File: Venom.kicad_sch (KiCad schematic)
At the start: 12 parts, among them CN1 HC-XH-5A-G, CN2 HC-PH-8A-G, CN3 HC-XH-8A-G, CN4 HC-XH-8A-G, CN5 HC-XH-2A-G, CN6 HC-PH-7A-G, U1 Pico

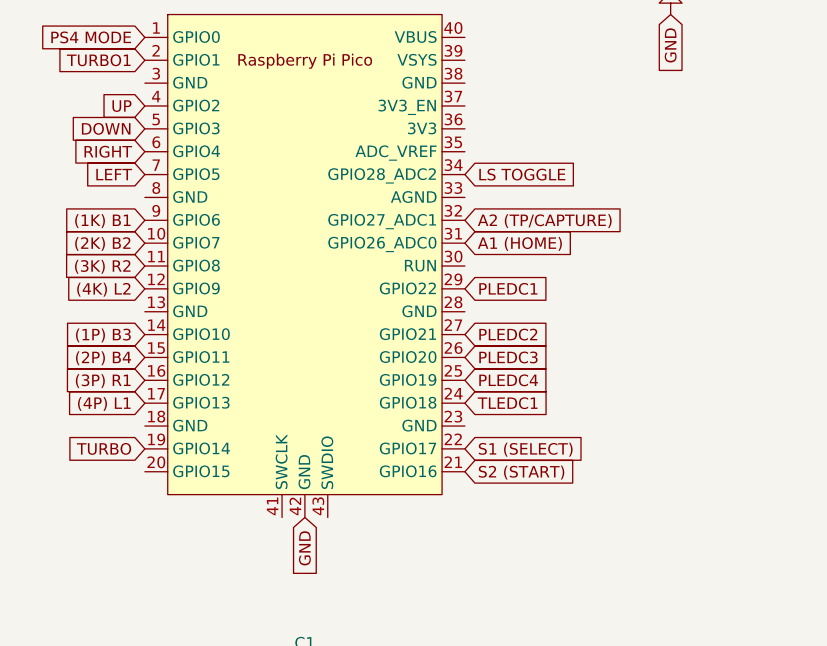
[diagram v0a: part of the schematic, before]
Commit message: Add ground fill
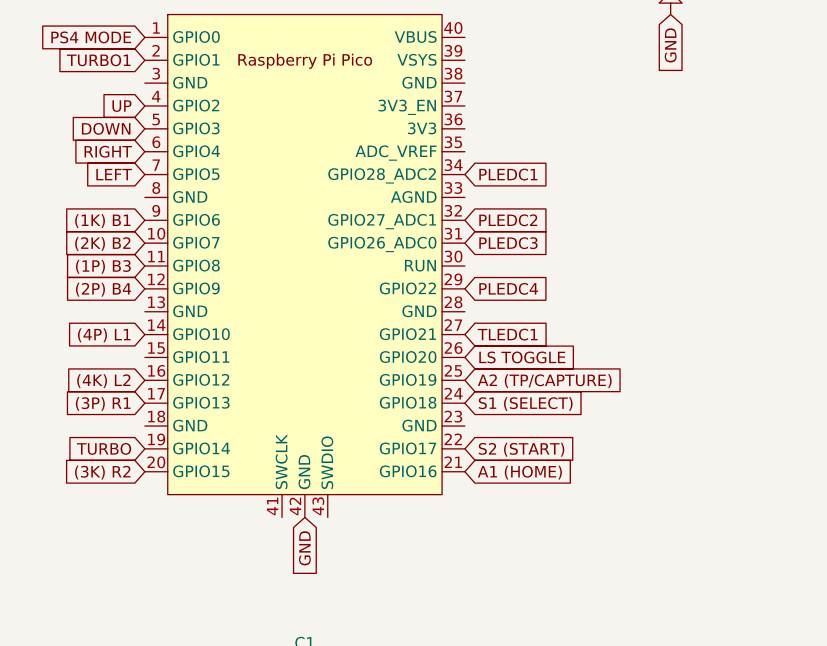
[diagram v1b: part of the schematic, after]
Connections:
- net (1P) B3: now also U1.11 (GPIO8); no longer U1.14 (GPIO10)
- net (2P) B4: now also U1.12 (GPIO9); no longer U1.15 (GPIO11)
- net (3K) R2: now also U1.20 (GPIO15); no longer U1.11 (GPIO8)
- net (3P) R1: now also U1.17 (GPIO13); no longer U1.16 (GPIO12)
- net (4K) L2: now also U1.16 (GPIO12); no longer U1.12 (GPIO9)
- net (4P) L1: now also U1.14 (GPIO10); no longer U1.17 (GPIO13)
- net A1 (HOME): now also U1.21 (GPIO16); no longer U1.31 (GPIO26_ADC0)
- net A2 (TP/CAPTURE): now also U1.25 (GPIO19); no longer U1.32 (GPIO27_ADC1)
- net LS TOGGLE: now also U1.26 (GPIO20); no longer U1.34 (GPIO28_ADC2)
- net PLEDC1: now also U1.34 (GPIO28_ADC2); no longer U1.29 (GPIO22)
- net PLEDC2: now also U1.32 (GPIO27_ADC1); no longer U1.27 (GPIO21)
- net PLEDC3: now also U1.31 (GPIO26_ADC0); no longer U1.26 (GPIO20)
- net PLEDC4: now also U1.29 (GPIO22); no longer U1.25 (GPIO19)
- net S1 (SELECT): now also U1.24 (GPIO18); no longer U1.22 (GPIO17)
- net S2 (START): now also U1.22 (GPIO17); no longer U1.21 (GPIO16)
- net TLEDC1: now also U1.27 (GPIO21); no longer U1.24 (GPIO18)

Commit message: Add WEB button
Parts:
- added SW1: GT-TC030A-H020-L1N, easyeda2kicad:SW-SMD_4P-L3.6-W3.0-P1.50-LS4.7, symbol easyeda2kicad:GT-TC030A-H020-L1N
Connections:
- net GND: now also SW1.4
- net S2 (START): now also SW1.1
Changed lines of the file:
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@@
+    )
+  )
+  (global_label "GND" (shape input) (at 210.82 33.02 0) (fields_autoplaced)
+    (effects (font (size 1.27 1.27)) (justify left))
+    (property "Intersheetrefs" "${INTERSHEET_REFS}" (at 217.5963 33.02 0)
+      (effects (font (size 1.27 1.27)) (justify left) hide)
     )
   )
@@
     (effects (font (size 1.27 1.27)) (justify right))
     (property "Intersheetrefs" "${INTERSHEET_REFS}" (at 20.1961 30.48 0)
+      (effects (font (size 1.27 1.27)) (justify right) hide)
+    )
+  )
+  (global_label "S2 (START)" (shape input) (at 195.58 27.94 180) (fields_autoplaced)
+    (effects (font (size 1.27 1.27)) (justify right))
+    (property "Intersheetrefs" "${INTERSHEET_REFS}" (at 182.0909 27.94 0)
       (effects (font (size 1.27 1.27)) (justify right) hide)
     )
@@
         )
       )
+    )
+  )
+  (symbol (lib_id "easyeda2kicad:GT-TC030A-H020-L1N") (at 203.2 30.48 0) (unit 1)
+    (in_bom yes) (on_board yes) (dnp no) (fields_autoplaced)
+    (property "Reference" "SW1" (at 203.2 22.86 0)
+      (effects (font (size 1.27 1.27)))
+    )
+    (property "Value" "GT-TC030A-H020-L1N" (at 203.2 25.4 0)
+      (effects (font (size 1.27 1.27)))
+    )
+    (property "Footprint" "easyeda2kicad:SW-SMD_4P-L3.6-W3.0-P1.50-LS4.7" (at 203.2 40.64 0)
+      (effects (font (size 1.27 1.27)) hide)
+    )
+    (property "Datasheet" "" (at 203.2 30.48 0)
+      (effects (font (size 1.27 1.27)) hide)
+    )
+    (property "Manufacturer" "G-Switch(品赞)" (at 203.2 43.18 0)
+      (effects (font (size 1.27 1.27)) hide)
+    )
+    (property "LCSC Part" "C843670" (at 203.2 45.72 0)
+      (effects (font (size 1.27 1.27)) hide)
+    )
+    (property "JLC Part" "Extended Part" (at 203.2 48.26 0)
+      (effects (font (size 1.27 1.27)) hide)
+    )
+    (pin "1")
+    (pin "2")
+    (pin "3")
+    (pin "4")
+    (instances
+      (project "Venom"
+        (path "/9bda465f-e399-4153-b93d-135c505ebd4f"
+          (reference "SW1") (unit 1)
+        )
+      )

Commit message: Add RESET button
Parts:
- added SW2: GT-TC030A-H020-L1N, easyeda2kicad:SW-SMD_4P-L3.6-W3.0-P1.50-LS4.7, symbol easyeda2kicad:GT-TC030A-H020-L1N
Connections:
- net GND: now also SW2.4
- net RUN: now reaches U1.30 (RUN)
- net RUN: now also SW2.1
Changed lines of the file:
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@@
+    )
+  )
+  (global_label "GND" (shape input) (at 210.82 48.26 0) (fields_autoplaced)
+    (effects (font (size 1.27 1.27)) (justify left))
+    (property "Intersheetrefs" "${INTERSHEET_REFS}" (at 204.0437 48.26 0)
+      (effects (font (size 1.27 1.27)) (justify right) hide)
     )
   )
@@
     )
   )
+  (global_label "RUN" (shape input) (at 66.04 53.34 0) (fields_autoplaced)
+    (effects (font (size 1.27 1.27)) (justify left))
+    (property "Intersheetrefs" "${INTERSHEET_REFS}" (at 72.8768 53.34 0)
+      (effects (font (size 1.27 1.27)) (justify left) hide)
+    )
+  )
   (global_label "PLED 2" (shape input) (at 52.07 113.03 0) (fields_autoplaced)
     (effects (font (size 1.27 1.27)) (justify left))
@@
     (effects (font (size 1.27 1.27)) (justify right))
     (property "Intersheetrefs" "${INTERSHEET_REFS}" (at 22.1918 38.1 0)
+      (effects (font (size 1.27 1.27)) (justify right) hide)
+    )
+  )
+  (global_label "RUN" (shape input) (at 195.58 43.18 180) (fields_autoplaced)
+    (effects (font (size 1.27 1.27)) (justify right))
+    (property "Intersheetrefs" "${INTERSHEET_REFS}" (at 188.7432 43.18 0)
       (effects (font (size 1.27 1.27)) (justify right) hide)
     )
@@
         )
       )
+    )
+  )
+  (symbol (lib_id "easyeda2kicad:GT-TC030A-H020-L1N") (at 203.2 45.72 0) (unit 1)
+    (in_bom yes) (on_board yes) (dnp no) (fields_autoplaced)
+    (property "Reference" "SW2" (at 203.2 38.1 0)
+      (effects (font (size 1.27 1.27)))
+    )
+    (property "Value" "GT-TC030A-H020-L1N" (at 203.2 40.64 0)
+      (effects (font (size 1.27 1.27)))
+    )
+    (property "Footprint" "easyeda2kicad:SW-SMD_4P-L3.6-W3.0-P1.50-LS4.7" (at 203.2 55.88 0)
+      (effects (font (size 1.27 1.27)) hide)
+    )
+    (property "Datasheet" "" (at 203.2 45.72 0)
+      (effects (font (size 1.27 1.27)) hide)
+    )
+    (property "Manufacturer" "G-Switch(品赞)" (at 203.2 58.42 0)
+      (effects (font (size 1.27 1.27)) hide)
+    )
+    (property "LCSC Part" "C843670" (at 203.2 60.96 0)
+      (effects (font (size 1.27 1.27)) hide)
+    )
+    (property "JLC Part" "Extended Part" (at 203.2 63.5 0)
+      (effects (font (size 1.27 1.27)) hide)
+    )
+    (pin "1")
+    (pin "2")
+    (pin "3")
+    (pin "4")
+    (instances
+      (project "Venom"
+        (path "/9bda465f-e399-4153-b93d-135c505ebd4f"
+          (reference "SW2") (unit 1)
+        )
+      )

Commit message: LEDs need a resistor not capacitor?
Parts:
- removed C1, C2, C3, C4, C5: CL05B103KB5NNNC, easyeda2kicad:C0402, symbol easyeda2kicad:CL05B103KB5NNNC
- added R1, R2, R3, R4, R5: 0603WAF3300T5E, easyeda2kicad:R0603, symbol easyeda2kicad:0603WAF3300T5E
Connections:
- net PLED 1: now also R1.2
- net PLED 2: now also R2.2
- net PLED 3: now also R3.2
- net PLED 4: now also R4.2
- net TURBO LED: now also R5.2
- net PLEDC1 renamed PLEDR1
- net PLEDR1: now also R1.1
- net PLEDC2 renamed PLEDR2
- net PLEDR2: now also R2.1
- net PLEDC3 renamed PLEDR3
- net PLEDR3: now also R3.1
- net PLEDC4 renamed PLEDR4
- net PLEDR4: now also R4.1
- net TLEDC1 renamed TLEDR1
- net TLEDR1: now also R5.1

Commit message: Change silk
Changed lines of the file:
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@@
   (global_label "GND" (shape input) (at 210.82 48.26 0) (fields_autoplaced)
     (effects (font (size 1.27 1.27)) (justify left))
-    (property "Intersheetrefs" "${INTERSHEET_REFS}" (at 204.0437 48.26 0)
-      (effects (font (size 1.27 1.27)) (justify right) hide)
+    (property "Intersheetrefs" "${INTERSHEET_REFS}" (at 217.5963 48.26 0)
+      (effects (font (size 1.27 1.27)) (justify left) hide)
     )
   )
@@
     )
   )
+  (global_label "GND" (shape input) (at 48.26 81.28 270) (fields_autoplaced)
+    (effects (font (size 1.27 1.27)) (justify right))
+    (property "Intersheetrefs" "${INTERSHEET_REFS}" (at 48.26 88.0563 90)
+      (effects (font (size 1.27 1.27)) (justify right) hide)
+    )
+  )
   (global_label "GND" (shape input) (at 158.75 67.31 180) (fields_autoplaced)
     (effects (font (size 1.27 1.27)) (justify right))
@@
     )
   )
-  (global_label "GND" (shape input) (at 88.9 25.4 270) (fields_autoplaced)
-    (effects (font (size 1.27 1.27)) (justify right))
-    (property "Intersheetrefs" "${INTERSHEET_REFS}" (at 88.9 32.1763 90)
-      (effects (font (size 1.27 1.27)) (justify right) hide)
-    )
-  )
   (global_label "PLEDR1" (shape input) (at 66.04 43.18 0) (fields_autoplaced)
     (effects (font (size 1.27 1.27)) (justify left))
@@
       (effects (font (size 1.27 1.27)) (justify right) hide)
     )
-  )
-  (global_label "GND" (shape input) (at 48.26 81.28 270) (fields_autoplaced)
-    (effects (font (size 1.27 1.27)) (justify right))
-    (property "Intersheetrefs" "${INTERSHEET_REFS}" (at 48.26 88.0563 90)
-      (effects (font (size 1.27 1.27)) (justify right) hide)
-    )

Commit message: WIP embedded design
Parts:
- removed R1, R2, R3, R4, R5: 0603WAF3300T5E, easyeda2kicad:R0603, symbol easyeda2kicad:0603WAF3300T5E
- removed U1: Pico, MCU_RaspberryPi_and_Boards:RPi_Pico_SMD_TH, symbol MCU_RaspberryPi_and_Boards:Pico
- added C1, C10, C4, C8: 1u, Capacitor_SMD:C_0402_1005Metric, symbol Device:C_Small
- added C11, C12, C13, C14, C15, C16, C5, C6, C7, C9: 100n, Capacitor_SMD:C_0402_1005Metric, symbol Device:C_Small
- added C2, C3: 30p, Capacitor_SMD:C_0402_1005Metric, symbol Device:C_Small
- added R1, R5: 1k, Resistor_SMD:R_0402_1005Metric, symbol Device:R_Small
- added R2: 10k, Resistor_SMD:R_0402_1005Metric, symbol Device:R_Small
- added R3, R4: 27, Resistor_SMD:R_0402_1005Metric, symbol Device:R_Small
- added R6, R7: 5.1k, Resistor_SMD:R_0402_1005Metric, symbol Device:R_Small
- added SW3: GT-TC030A-H020-L1N, easyeda2kicad:SW-SMD_4P-L3.6-W3.0-P1.50-LS4.7, symbol easyeda2kicad:GT-TC030A-H020-L1N
- added U1: TLV73333PDBV, Package_TO_SOT_SMD:SOT-23-5, symbol Regulator_Linear:TLV73333PDBV
- added U2: W25Q128JVS, Package_SO:SOIC-8_5.23x5.23mm_P1.27mm, symbol Flatbox-rev4-rescue:W25Q128JVS-Memory_Flash
- added U3: RP2040, RP2040:RP2040-QFN-56, symbol RP2040:RP2040
- added USB1: HRO-TYPE-C-31-M-12, Type-C:HRO-TYPE-C-31-M-12-Assembly, symbol Type-C:HRO-TYPE-C-31-M-12
- added Y1: Crystal_GND24, Crystal:Crystal_SMD_3225-4Pin_3.2x2.5mm, symbol Device:Crystal_GND24
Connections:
- net (1K) B1: now also U3.30 (GPIO19)
- net (1P) B3: now also U3.28 (GPIO17)
- net (2K) B2: now also U3.29 (GPIO18)
- net (2P) B4: now also U3.27 (GPIO16)
- net (3K) R2: now also U3.15 (GPIO12)
- net (3P) R1: now also U3.16 (GPIO13)
- net (4K) L2: now also U3.17 (GPIO14)
- net (4P) L1: now also U3.18 (GPIO15)
- net A1 (HOME): now also U3.9 (GPIO7)
- net A2 (TP/CAPTURE): now also U3.4 (GPIO2)
- net DOWN: now also U3.13 (GPIO10)
- net GND: now also C1.2, C10.2, C11.2, C12.2, C13.2, C14.2, C15.2, C16.2, C2.1, C3.2, C4.2, C5.2, C6.2, C7.2, C8.2, C9.2, R6.2, R7.2, SW3.4, U1.2 (GND), U2.4 (GND), U3.19 (TESTEN), U3.57 (GND), USB1.1 (GND), USB1.12 (GND), USB1.13 (SHIELD), Y1.2, Y1.4
- net LEFT: now also U3.11 (GPIO8)
- net LS TOGGLE: now also U3.6 (GPIO4)
- net PLED 1: now also U3.36 (GPIO24)
- net PLED 2: now also U3.35 (GPIO23)
- net PLED 3: now also U3.34 (GPIO22)
- net PLED 4: now also U3.32 (GPIO21)
- net PS4 MODE: now also U3.8 (GPIO6)
- net RIGHT: now also U3.12 (GPIO9)
- net RUN: now also U3.26 (RUN)
- net S1 (SELECT): now also U3.3 (GPIO1)
- net S2 (START): now also U3.2 (GPIO0)
- net TURBO: now also U3.5 (GPIO3)
- net TURBO LED: now also U3.31 (GPIO20)
- net TURBO1: now also U3.7 (GPIO5)
- net UP: now also U3.14 (GPIO11)
- new net: R7.1, USB1.4 (CC1)
- new net: R6.1, USB1.10 (CC2)
- new net: C3.1, R5.1, Y1.3
- new net: R4.2, U3.46 (USB_DM)
- new net: R3.2, U3.47 (USB_DP)
- new net +1V1: C6.1, C7.1, C8.1, U3.23 (DVDD), U3.45 (VREG_VOUT), U3.50 (DVDD)
- new net +3V3: C10.1, C11.1, C12.1, C13.1, C14.1, C15.1, C16.1, C4.1, C5.1, C9.1, R2.1, U1.5 (OUT), U2.8 (VCC), U3.1 (IOVDD), U3.10 (IOVDD), U3.22 (IOVDD), U3.33 (IOVDD), U3.42 (IOVDD), U3.43 (ADC_AVDD), U3.44 (VREG_IN), U3.48 (USB_VDD), U3.49 (IOVDD)
- new net +5V: C1.1, U1.1 (IN), U1.3 (EN), USB1.11 (VBUS), USB1.2 (VBUS)
- new net BOOTSEL: R1.2, SW3.1
- new net D+: R3.1, USB1.6 (DP1), USB1.8 (DP2)
- new net D-: R4.1, USB1.5 (DN2), USB1.7 (DN1)
- new net QSPI_SCLK: U2.6 (CLK), U3.52 (QSPI_SCLK)
- new net QSPI_SD0: U2.5 (DI(IO0)), U3.53 (QSPI_SD0)
- new net QSPI_SD1: U2.2 (DO(IO1)), U3.55 (QSPI_SD1)
- new net QSPI_SD2: U2.3 (IO2), U3.54 (QSPI_SD2)
- new net QSPI_SD3: U2.7 (IO3), U3.51 (QSPI_SD3)
- new net QSPI_SS: R1.1, R2.2, U2.1 (~{CS}), U3.56 (QSPI_SS)
- new net XIN: C2.2, U3.20 (XIN), Y1.1
- new net XOUT: R5.2, U3.21 (XOUT)
- no-connect marks 0 -> 9
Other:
- note added: "Crystal"
- note added: "Flash"
- note added: "Make sure C10 is close to pin 44 of RP2040"
- note added: "Make sure C8 is close to pin 45 of RP2040"
- note added: "Power"
- note added: "USB"
- moved on the sheet: CN1, CN2, CN3, CN4, CN5, CN6, SW1, SW2

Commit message: Nearly all wired up?
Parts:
- removed U2: W25Q128JVS, Package_SO:SOIC-8_5.23x5.23mm_P1.27mm, symbol Flatbox-rev4-rescue:W25Q128JVS-Memory_Flash
- added U2: W25Q128JVSIQTR, easyeda2kicad:SOIC-8_L5.3-W5.3-P1.27-LS8.0-BL, symbol easyeda2kicad:W25Q128JVSIQTR
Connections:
- net (1K) B1: now also U3.7 (GPIO5); no longer U3.30 (GPIO19)
- net (1P) B3: now also U3.9 (GPIO7); no longer U3.28 (GPIO17)
- net (2K) B2: now also U3.8 (GPIO6); no longer U3.29 (GPIO18)
- net (2P) B4: now also U3.11 (GPIO8); no longer U3.27 (GPIO16)
- net (3K) R2: now also U3.16 (GPIO13); no longer U3.15 (GPIO12)
- net (3P) R1: now also U3.15 (GPIO12); no longer U3.16 (GPIO13)
- net (4K) L2: now also U3.14 (GPIO11); no longer U3.17 (GPIO14)
- net (4P) L1: now also U3.13 (GPIO10); no longer U3.18 (GPIO15)
- net +3V3: now also U2.8 (VCC)
- net A1 (HOME): now also U3.12 (GPIO9); no longer U3.9 (GPIO7)
- net A2 (TP/CAPTURE): now also U3.31 (GPIO20); no longer U3.4 (GPIO2)
- net DOWN: now also U3.27 (GPIO16); no longer U3.13 (GPIO10)
- net GND: now also U2.4 (GND)
- net LEFT: now also U3.17 (GPIO14); no longer U3.11 (GPIO8)
- net LS TOGGLE: now also U3.34 (GPIO22); no longer U3.6 (GPIO4)
- net PLED 1: now also U3.41 (GPIO29_ADC3); no longer U3.36 (GPIO24)
- net PLED 2: now also U3.40 (GPIO28_ADC2); no longer U3.35 (GPIO23)
- net PLED 3: now also U3.39 (GPIO27_ADC1); no longer U3.34 (GPIO22)
- net PLED 4: now also U3.38 (GPIO26_ADC0); no longer U3.32 (GPIO21)
- net PS4 MODE: now also U3.36 (GPIO24); no longer U3.8 (GPIO6)
- net QSPI_SCLK: now also U2.6 (CLK)
- net QSPI_SD0: now also U2.5 (DI)
- net QSPI_SD1: now also U2.2 (DO)
- net QSPI_SD2: now also U2.3 (IO2)
- net QSPI_SD3: now also U2.7 (IO3)
- net QSPI_SS: now also U2.1 (~{CS})
- net RIGHT: now also U3.18 (GPIO15); no longer U3.12 (GPIO9)
- net S1 (SELECT): now also U3.30 (GPIO19); no longer U3.3 (GPIO1)
- net S2 (START): now also U3.29 (GPIO18); no longer U3.2 (GPIO0)
- net TURBO: now also U3.32 (GPIO21); no longer U3.5 (GPIO3)
- net TURBO LED: now also U3.37 (GPIO25); no longer U3.31 (GPIO20)
- net TURBO1: now also U3.35 (GPIO23); no longer U3.7 (GPIO5)
- net UP: now also U3.28 (GPIO17); no longer U3.14 (GPIO11)
- no-connect marks 9 -> 16

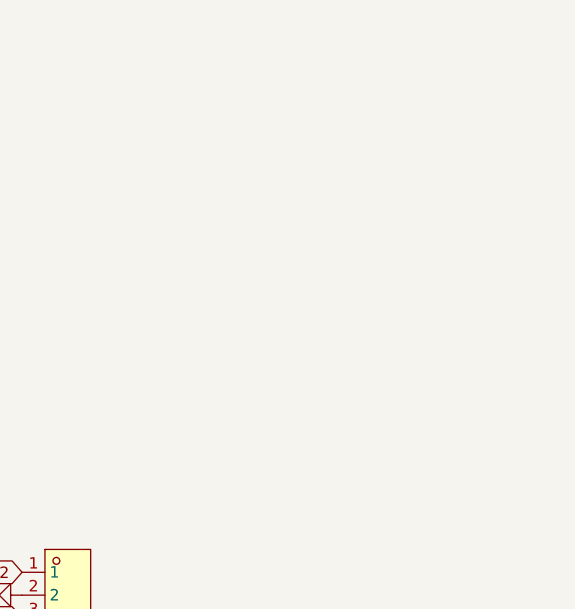
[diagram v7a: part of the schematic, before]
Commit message: Add individual up, down, left and right connectors
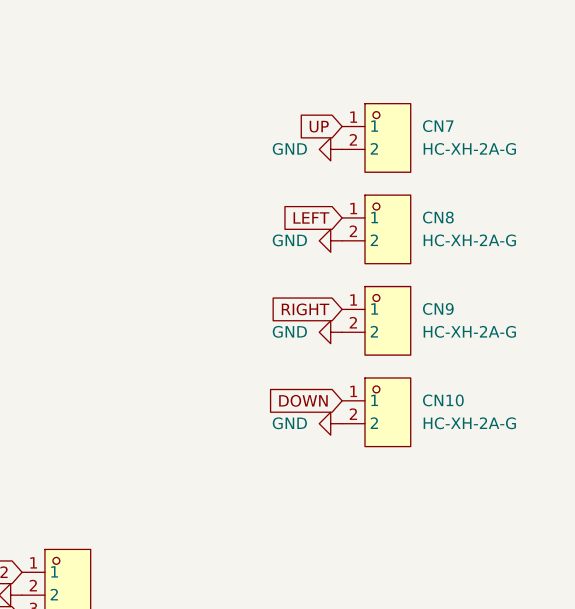
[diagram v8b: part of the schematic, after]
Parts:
- added CN10, CN7, CN8, CN9: HC-XH-2A-G, easyeda2kicad:CONN-TH_2P-P2.50_HC-XH-2A-G, symbol easyeda2kicad:HC-XH-2A-G
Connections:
- net DOWN: now also CN10.1
- net GND: now also CN10.2, CN7.2, CN8.2, CN9.2
- net LEFT: now also CN8.1
- net RIGHT: now also CN9.1
- net UP: now also CN7.1
